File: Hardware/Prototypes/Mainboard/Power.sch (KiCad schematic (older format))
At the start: 15 parts, among them J2 LiPo, J3 BAT_V, J4 BAT_T, J5 +5V, U1 OSD3358-512M-BCB

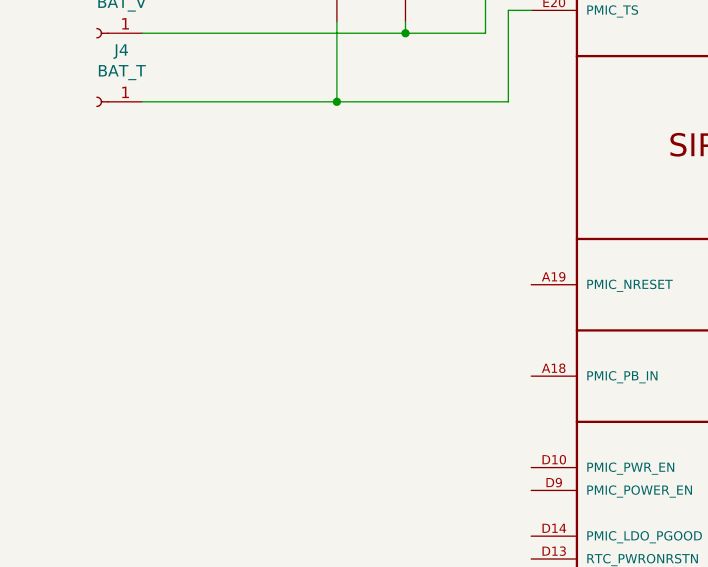
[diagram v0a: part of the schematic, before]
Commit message: Added PMIC_NRESET
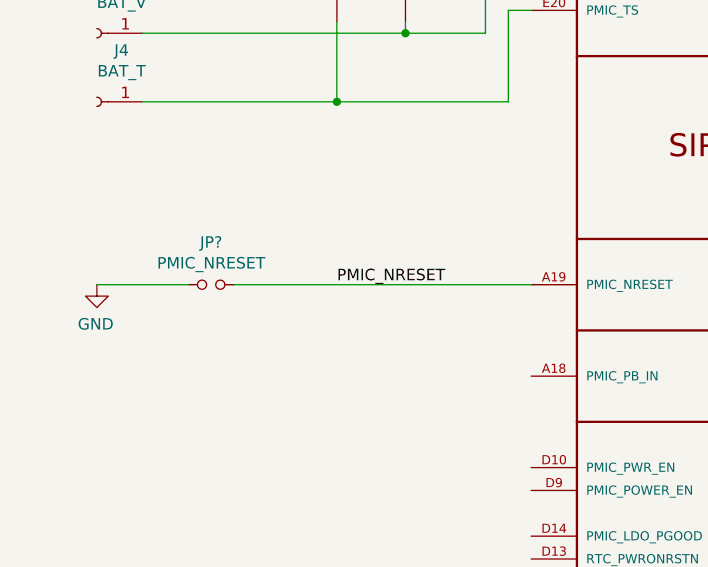
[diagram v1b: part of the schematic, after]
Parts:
- added JP?: PMIC_NRESET, Connector_PinHeader_2.54mm:PinHeader_1x02_P2.54mm_Vertical, symbol Device:Jumper_NO_Small
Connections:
- net GND: now also JP?.1
- net PMIC_NRESET: now reaches U1.A19 (PMIC_NRESET)
- net PMIC_NRESET: now also JP?.2
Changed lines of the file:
@@
 	13900 7550 13900 7650
 Connection ~ 13900 7650
+$Comp
+L power:GND #PWR?
+U 1 1 5D5C3E92
+P 1750 4650
+AR Path="/5D5C3E92" Ref="#PWR?"  Part="1"
+AR Path="/5D5C5718/5D5C3E92" Ref="#PWR?"  Part="1"
+F 0 "#PWR?" H 1750 4400 50  0001 C CNN
+F 1 "GND" H 1755 4477 50  0000 C CNN
+F 2 "" H 1750 4650 50  0001 C CNN
+F 3 "" H 1750 4650 50  0001 C CNN
+	1    1750 4650
+	-1   0    0    -1
+$EndComp
+Wire Wire Line
+	2150 4650 1750 4650
+Wire Wire Line
+	3650 4650 2350 4650
+Text Label 2800 4650 0    50   ~ 0
+PMIC_NRESET
+$Comp
+L Device:Jumper_NO_Small JP?
+U 1 1 5D62B518
+P 2250 4650
+F 0 "JP?" H 2250 4835 50  0000 C CNN
+F 1 "PMIC_NRESET" H 2250 4744 50  0000 C CNN
+F 2 "Connector_PinHeader_2.54mm:PinHeader_1x02_P2.54mm_Vertical" H 2250 4650 50  0001 C CNN
+F 3 "~" H 2250 4650 50  0001 C CNN
+	1    2250 4650
+	1    0    0    -1
+$EndComp
 $EndSCHEMATC

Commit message: More work
Still on the power section. Next - clamping circuit!
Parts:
- removed JP?: PMIC_NRESET, Connector_PinHeader_2.54mm:PinHeader_1x02_P2.54mm_Vertical, symbol Device:Jumper_NO_Small
- added D?: LED, LED_SMD:LED_0603_1608Metric_Castellated, symbol Device:LED
- added J6: I2C0, Connector_PinHeader_2.54mm:PinHeader_1x03_P2.54mm_Vertical, symbol Connector:Conn_01x03_Male
- added R1, R2: 1k5, Resistor_SMD:R_0603_1608Metric, symbol Device:R_Small
- added R?: R_Small, Resistor_SMD:R_0603_1608Metric, symbol Device:R_Small
- added SW1: POWER, Button_Switch_SMD:SW_SPST_B3SL-1002P, symbol Switch:SW_Push
- added TP10: NINT, TestPoint:TestPoint_Pad_D1.0mm, symbol Connector:TestPoint
- added TP7: PWREN, TestPoint:TestPoint_Pad_D1.0mm, symbol Connector:TestPoint
- added TP8: LPGD, TestPoint:TestPoint_Pad_D1.0mm, symbol Connector:TestPoint
- added TP9: NWKP, TestPoint:TestPoint_Pad_D1.0mm, symbol Connector:TestPoint
- added TP?: VDD2_3P3V, TestPoint:TestPoint_Pad_D1.0mm, symbol Connector:TestPoint
- added TP?: PMIC_NRESET, TestPoint:TestPoint_Pad_D1.0mm, symbol Connector:TestPoint
- TP11: renamed from TP7; footprint TestPoint:TestPoint_Keystone_5015_Micro-Minature -> TestPoint:TestPoint_Pad_D1.0mm
- TP12: renamed from TP8; footprint TestPoint:TestPoint_Keystone_5015_Micro-Minature -> TestPoint:TestPoint_Pad_D1.0mm
- TP13: renamed from TP9; footprint TestPoint:TestPoint_Keystone_5015_Micro-Minature -> TestPoint:TestPoint_Pad_D1.0mm
- TP2, TP3, TP4, TP5, TP6: footprint TestPoint:TestPoint_Keystone_5015_Micro-Minature -> TestPoint:TestPoint_Pad_D1.0mm
- U1: footprint OSD335X-BGA-400 -> OSD3358-512M-BCB:OSD335X-BGA-400
- renumbered R1 to R3
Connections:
- net GND: now also J6.1 (Pin_1), R?.1, SW1.1
- net PMIC_NRESET: now also TP?.1
- net SYS_VDD1_3P3V: now also R1.1, R2.1
- net PMIC_PB_IN: now reaches U1.A18 (PMIC_PB_IN)
- net PMIC_PB_IN: now also SW1.2
- net at U1.D10 (PMIC_PWR_EN): now also U1.D9 (PMIC_POWER_EN), TP7.1
- net at U1.D13 (RTC_PWRONRSTN): now also U1.D14 (PMIC_LDO_PGOOD), TP8.1
- net SYS_VDD2_3P3V: now reaches U1.F12 (SYS_VDD2_3P3V@1)
- net SYS_VDD2_3P3V: now also U1.F13 (SYS_VDD2_3P3V@2), U1.G12 (SYS_VDD2_3P3V@3), U1.G13 (SYS_VDD2_3P3V@4), D?.2 (A), TP?.1
- net at U1.G17 (PMIC_NWAKEUP): now also U1.H17 (EXT_WAKEUP), TP9.1
- net at U1.J17 (PMIC_NINT): now also U1.K17 (EXTINTN), TP10.1
- net I2C0_SDA: now reaches U1.U7 (PMIC_SDA)
- net I2C0_SDA: now also U1.V7 (I2C0_SDA), J6.3 (Pin_3), R1.2
- net I2C0_SCL: now reaches U1.U8 (PMIC_SCL)
- net I2C0_SCL: now also U1.V8 (I2C0_SCL), J6.2 (Pin_2), R2.2
- new net: D?.1 (K), R?.2
- no-connect marks 0 -> 1
